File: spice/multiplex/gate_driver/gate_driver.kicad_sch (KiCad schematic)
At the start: 10 parts, among them Q1 NMOS, Q2 PMOS

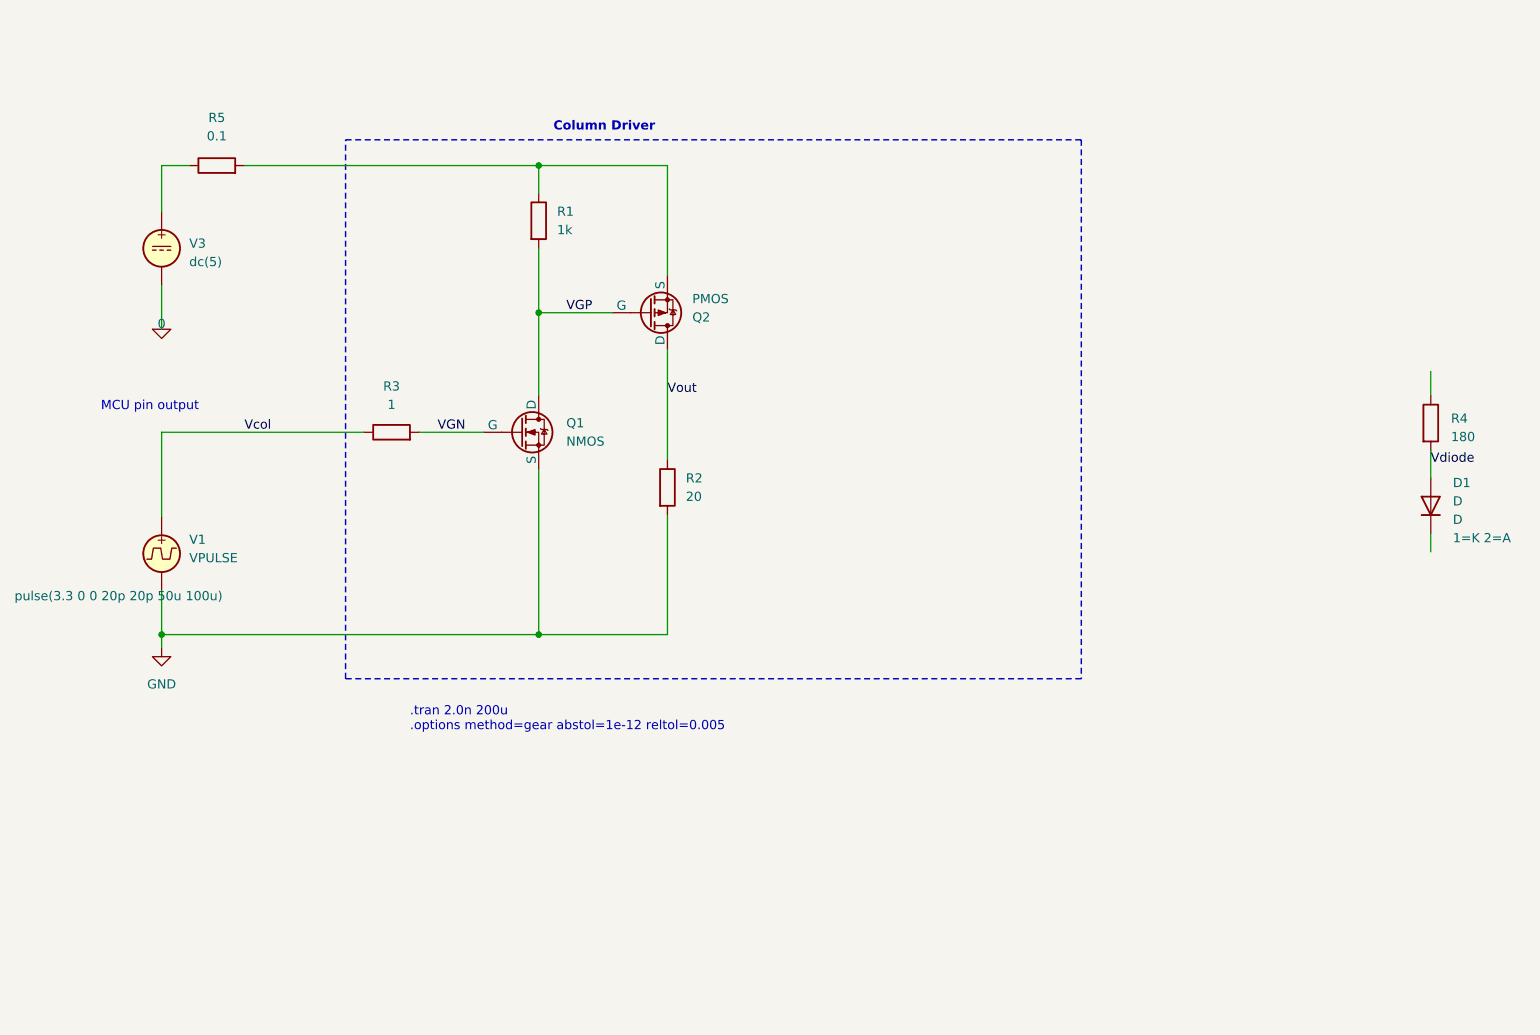
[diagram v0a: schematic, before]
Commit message: Added gate_driver simulation
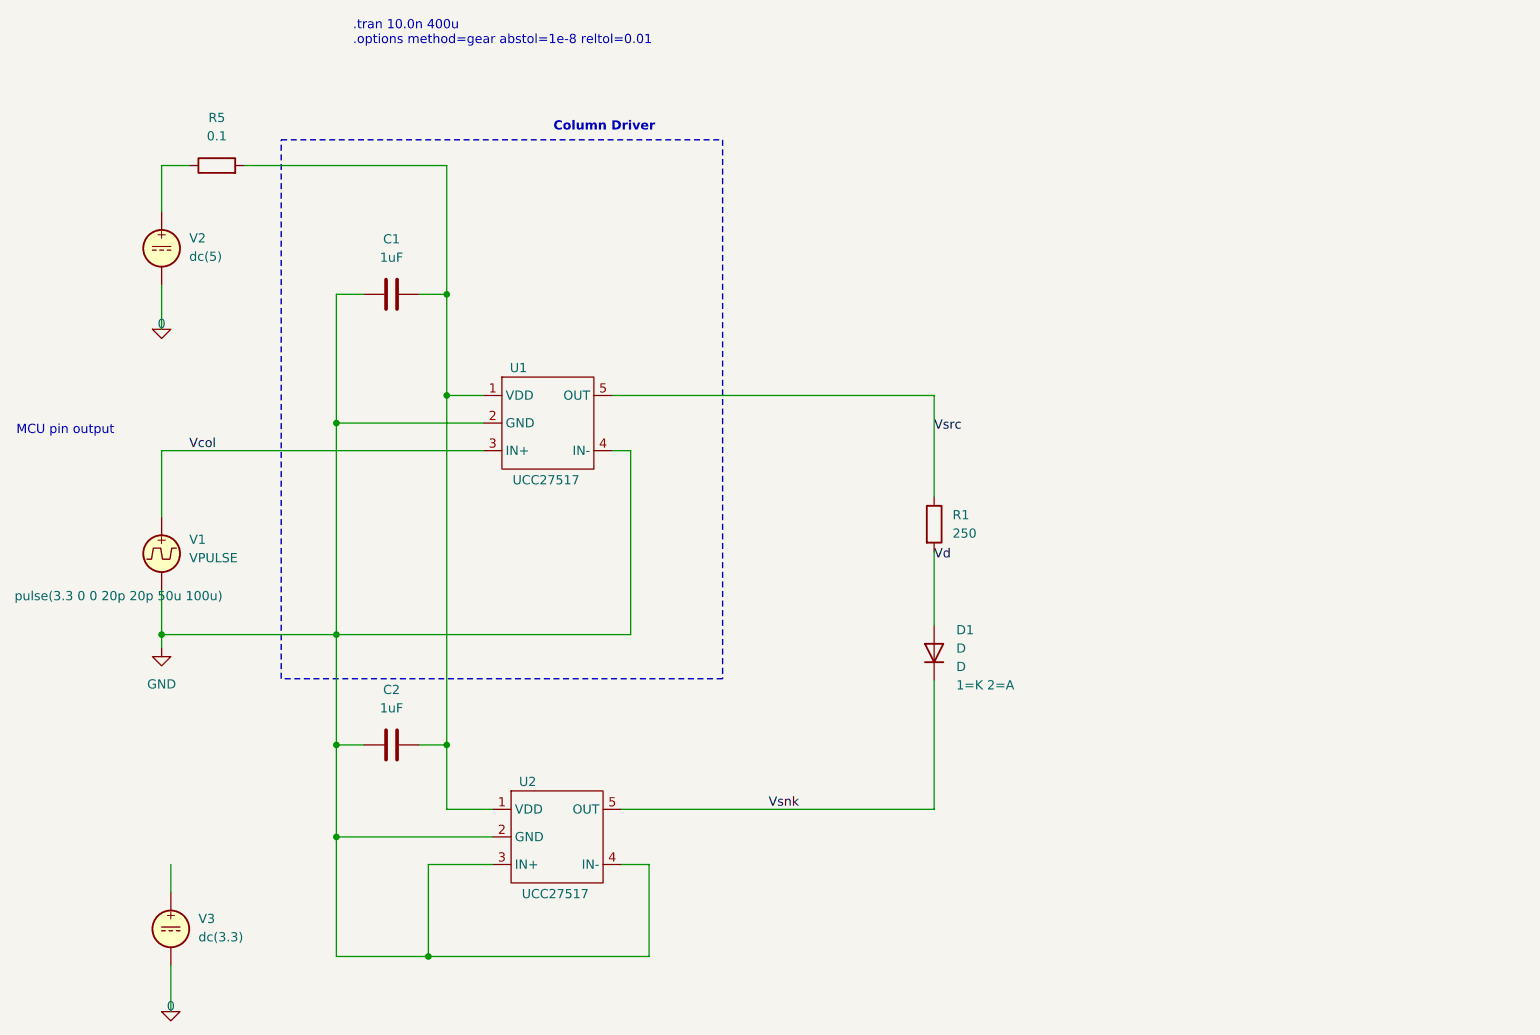
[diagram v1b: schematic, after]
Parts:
- removed Q1: NMOS, symbol Simulation_SPICE:NMOS
- removed Q2: PMOS, symbol Simulation_SPICE:PMOS
- removed R1: 1k, symbol Device:R
- removed R2: 20, symbol Device:R
- removed R3: 1, symbol Device:R
- added C1, C2: 1uF, symbol Device:C
- added U1, U2: UCC27517, symbol gate_driver:UCC27517
- added V3: dc(3.3), symbol Simulation_SPICE:VDC
- R1: renamed from R4; value 180 -> 250
- renumbered V3 to V2
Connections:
- net 0: now also V3.2
- net GND: now also C1.2, C2.1, U1.2 (GND), U1.4 (IN-), U2.2 (GND), U2.3 (IN+), U2.4 (IN-)
- net Vcol: now also U1.3 (IN+)
- net at R5.2: now also C1.1, C2.2, U1.1 (VDD), U2.1 (VDD)
- net Vsrc: now reaches R1.1
- net Vsrc: now also U1.5 (OUT)
- net Vsnk: now reaches D1.1 (K)
- net Vsnk: now also U2.5 (OUT)
- net Vdiode renamed Vd
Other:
- note added: ".tran 10.0n 400u .options method=gear abstol=1e-8 reltol=0.01"
- note removed: ".tran 2.0n 200u .options method=gear abstol=1e-12 reltol=0.005"
- moved on the sheet: D1, R1

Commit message: Worked on new 18x18 led version of rp2350 design.
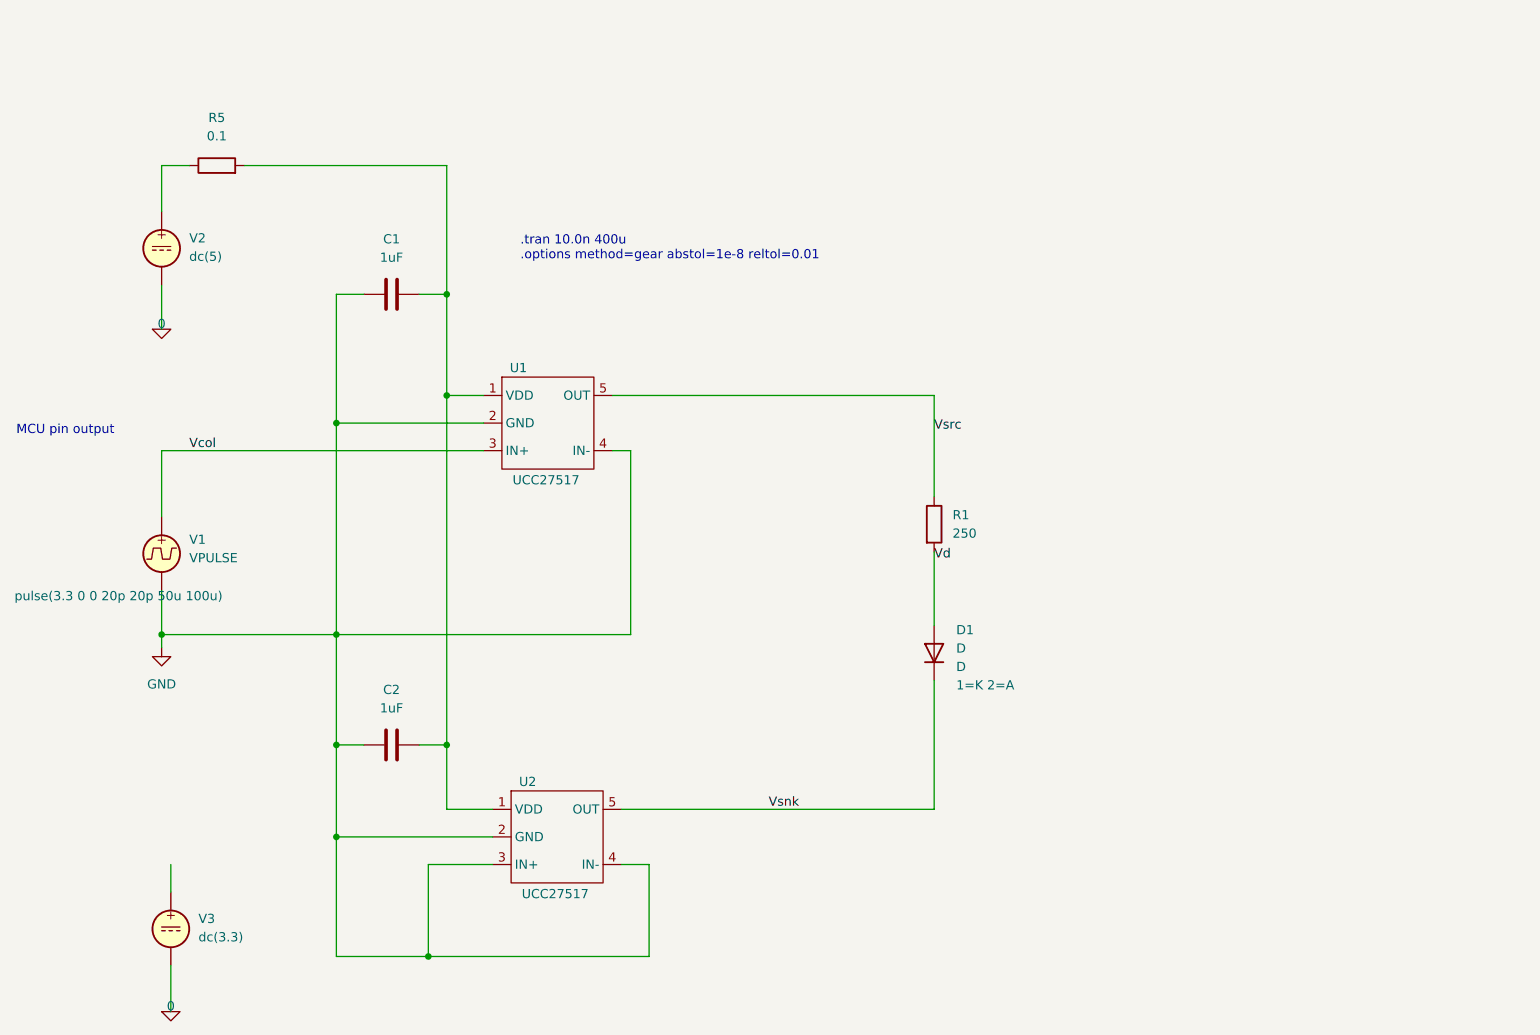
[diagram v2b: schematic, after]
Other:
- note removed: "Column Driver"
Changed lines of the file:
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@@
 	(generator_version "9.0")
 	(paper "A4")
-	(rectangle
-		(start 99.06 44.704)
-		(end 160.02 119.126)
-		(stroke
-			(width 0.2)
-			(type dash)
-		)
-		(fill
-			(type none)
-		)
-	)
 	(text "MCU pin output"
 		(exclude_from_sim no)
@@
 	(text ".tran 10.0n 400u\n.options method=gear abstol=1e-8 reltol=0.01"
 		(exclude_from_sim no)
-		(at 108.966 31.75 0)
+		(at 132.08 61.468 0)
 		(effects
 			(font
@@
 			)
 			(justify left bottom)
-		)
-	)
-	(text "Column Driver"
-		(exclude_from_sim no)
-		(at 136.652 43.688 0)
-		(effects
-			(font
-				(size 1.27 1.27)
-				(thickness 0.254)
-				(bold yes)
-			)
-			(justify left bottom)
